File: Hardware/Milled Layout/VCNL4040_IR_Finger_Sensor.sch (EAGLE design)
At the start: 9 parts, among them U1 VCNL4040

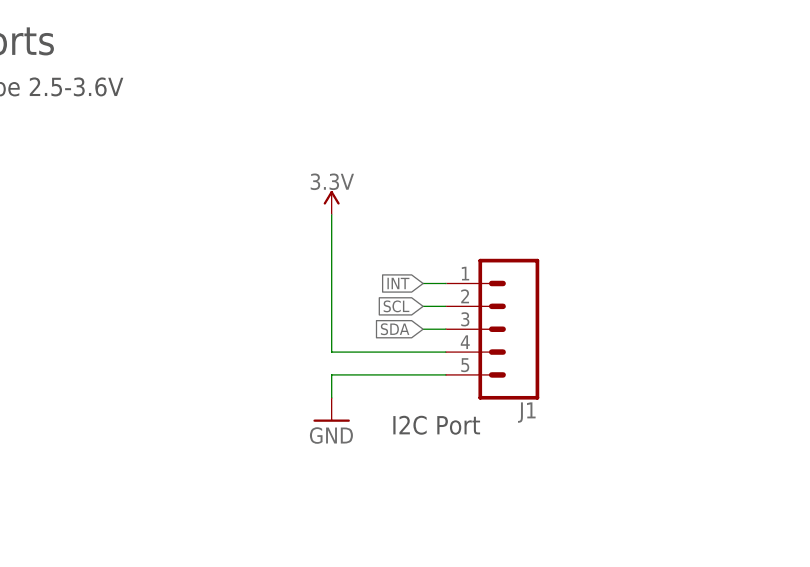
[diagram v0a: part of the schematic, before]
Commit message: Got rid of INT pin for Mill version
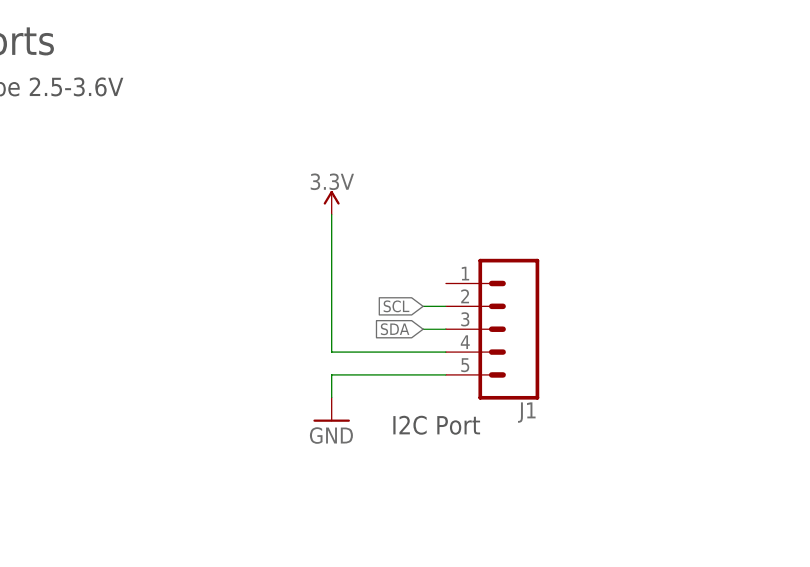
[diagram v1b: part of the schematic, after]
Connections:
- net INT: no longer J1.1
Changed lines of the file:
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@@
 <junction x="139.7" y="106.68"/>
-</segment>
-<segment>
-<wire x1="68.58" y1="33.02" x2="66.04" y2="33.02" width="0.1524" layer="91"/>
-<label x="66.04" y="33.02" size="1.27" layer="95" rot="R180" xref="yes"/>
-<pinref part="J1" gate="G$1" pin="1"/>
 </segment>
 </net>

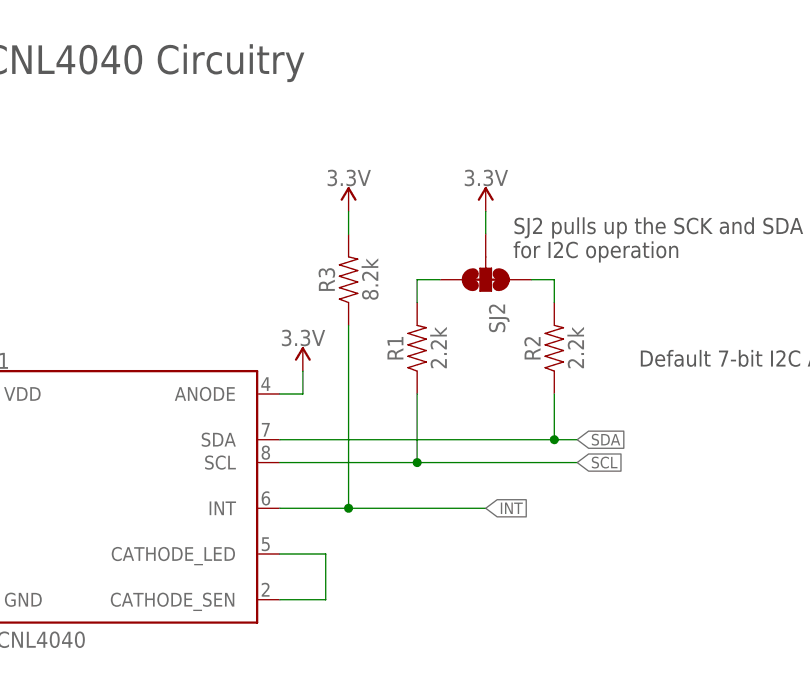
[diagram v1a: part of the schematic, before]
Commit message: New proto layout with no vias
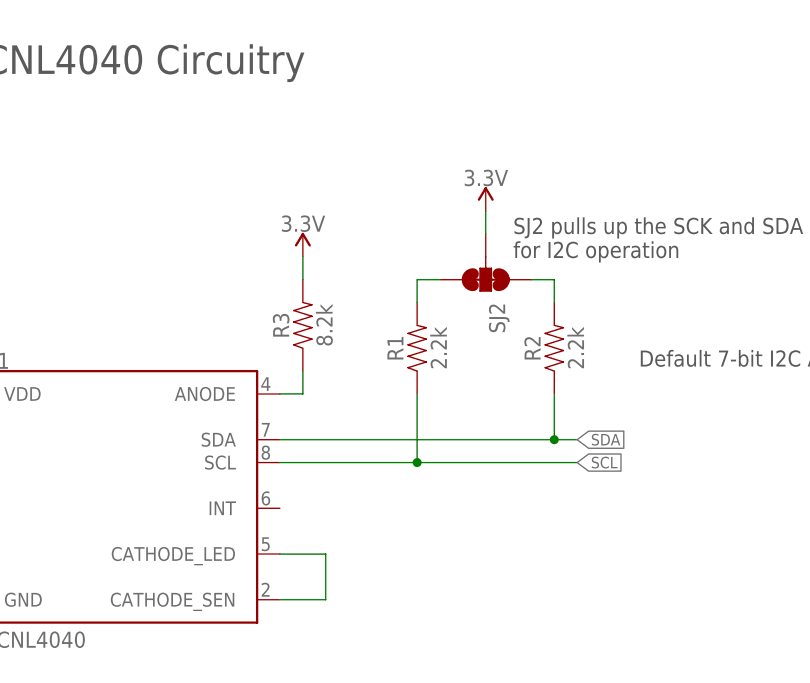
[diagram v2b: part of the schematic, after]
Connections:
- removed net INT: R3.1, U1.INT
- new net N$2: R3.1, U1.ANODE
- net 3.3V: no longer U1.ANODE
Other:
- moved on the sheet: R3
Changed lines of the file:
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@@
 <?xml version="1.0" encoding="utf-8"?>
 <!DOCTYPE eagle SYSTEM "eagle.dtd">
-<eagle version="7.6.0">
+<eagle version="7.7.0">
 <drawing>
 <settings>
@@
 <part name="J1" library="SparkFun-Connectors" deviceset="CONN_05" device=""/>
 <part name="R3" library="SparkFun-Resistors" deviceset="8.2KOHM" device="-0603-1/10W-5%" value="8.2k"/>
-<part name="SUPPLY4" library="SparkFun-PowerSymbols" deviceset="3.3V" device=""/>
 </parts>
 <sheets>
@@
 <instance part="SJ2" gate="G$1" x="154.94" y="132.08" rot="R270"/>
 <instance part="SUPPLY8" gate="G$1" x="55.88" y="40.64"/>
-<instance part="SUPPLY11" gate="G$1" x="134.62" y="121.92"/>
+<instance part="SUPPLY11" gate="G$1" x="134.62" y="134.62"/>
 <instance part="SUPPLY12" gate="G$1" x="154.94" y="139.7"/>
 <instance part="SUPPLY1" gate="G$1" x="93.98" y="121.92"/>
@@
 <instance part="U1" gate="G$1" x="114.3" y="109.22"/>
 <instance part="J1" gate="G$1" x="76.2" y="27.94" rot="R180"/>
-<instance part="R3" gate="G$1" x="139.7" y="132.08" rot="R90"/>
-<instance part="SUPPLY4" gate="G$1" x="139.7" y="139.7"/>
+<instance part="R3" gate="G$1" x="134.62" y="127" rot="R90"/>
 </instances>
 <busses>
@@
 </segment>
 </net>
-<net name="INT" class="0">
-<segment>
-<wire x1="132.08" y1="106.68" x2="139.7" y2="106.68" width="0.1524" layer="91"/>
-<label x="154.94" y="106.68" size="1.27" layer="95" xref="yes"/>
-<pinref part="U1" gate="G$1" pin="INT"/>
-<pinref part="R3" gate="G$1" pin="1"/>
-<wire x1="139.7" y1="106.68" x2="154.94" y2="106.68" width="0.1524" layer="91"/>
-<wire x1="139.7" y1="127" x2="139.7" y2="106.68" width="0.1524" layer="91"/>
-<junction x="139.7" y="106.68"/>
-</segment>
-</net>
 <net name="3.3V" class="0">
 <segment>
@@
 </segment>
 <segment>
+<pinref part="R3" gate="G$1" pin="2"/>
 <pinref part="SUPPLY11" gate="G$1" pin="3.3V"/>
-<pinref part="U1" gate="G$1" pin="ANODE"/>
-<wire x1="134.62" y1="121.92" x2="134.62" y2="119.38" width="0.1524" layer="91"/>
-<wire x1="134.62" y1="119.38" x2="132.08" y2="119.38" width="0.1524" layer="91"/>
-</segment>
-<segment>
-<pinref part="R3" gate="G$1" pin="2"/>
-<pinref part="SUPPLY4" gate="G$1" pin="3.3V"/>
-<wire x1="139.7" y1="137.16" x2="139.7" y2="139.7" width="0.1524" layer="91"/>
+<wire x1="134.62" y1="134.62" x2="134.62" y2="132.08" width="0.1524" layer="91"/>
 </segment>
 </net>
@@
 </segment>
 </net>
+<net name="N$2" class="0">
+<segment>
+<pinref part="U1" gate="G$1" pin="ANODE"/>
+<wire x1="134.62" y1="119.38" x2="132.08" y2="119.38" width="0.1524" layer="91"/>
+<pinref part="R3" gate="G$1" pin="1"/>
+<wire x1="134.62" y1="121.92" x2="134.62" y2="119.38" width="0.1524" layer="91"/>
+</segment>
+</net>

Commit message: Adding examples. Testing JST on milled layout.
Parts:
- removed R3: 8.2k, SparkFun-Resistors:8.2KOHM-0603-1/10W-5%
- removed SJ2: (no value), TestAperatures:JUMPER-PAD-3-NC_BY_TRACE
- added U$1, U$2: STAND-OFF, SparkX:STAND-OFF
- J1: device SparkFun-Connectors:CONN_05 -> SparkFun-Connectors:CONN_04SMD2
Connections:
- removed net N$2: R3.1, U1.ANODE
- removed net N$4: R2.2, SJ2.1
- removed net N$5: R1.2, SJ2.3
- net 3.3V: now also J1.2, R1.2, R2.2, U1.ANODE; no longer J1.4, R3.2, SJ2.2
- net GND: now also J1.1; no longer J1.5
- net SCL: now also J1.4; no longer J1.2
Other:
- note removed: "SJ2 pulls up the SCK and SDA lines for I2C operation"
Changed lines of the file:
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@@
 <part name="GND4" library="SparkFun" deviceset="GND" device=""/>
 <part name="C4" library="SparkFun-Capacitors" deviceset="0.1UF" device="-0603-25V-(+80/-20%)" value="0.1uF"/>
-<part name="SJ2" library="TestAperatures" deviceset="JUMPER-PAD-3-NC_BY_TRACE" device=""/>
 <part name="SUPPLY8" library="SparkFun-PowerSymbols" deviceset="3.3V" device=""/>
 <part name="SUPPLY11" library="SparkFun-PowerSymbols" deviceset="3.3V" device=""/>
@@
 <part name="GND8" library="SparkFun-PowerSymbols" deviceset="GND" device=""/>
 <part name="U1" library="SparkX" deviceset="VCNL4040" device=""/>
-<part name="J1" library="SparkFun-Connectors" deviceset="CONN_05" device=""/>
-<part name="R3" library="SparkFun-Resistors" deviceset="8.2KOHM" device="-0603-1/10W-5%" value="8.2k"/>
+<part name="U$1" library="SparkX" deviceset="STAND-OFF" device=""/>
+<part name="U$2" library="SparkX" deviceset="STAND-OFF" device=""/>
+<part name="J1" library="SparkFun-Connectors" deviceset="CONN_04" device="SMD2"/>
+<part name="SUPPLY4" library="SparkFun-PowerSymbols" deviceset="3.3V" device=""/>
 </parts>
 <sheets>
@@
 <text x="170.688" y="11.176" size="2.54" layer="94">Joel Bartlett</text>
 <text x="5.08" y="177.8" size="3.81" layer="97">VCNL4040 IR Finger Sensor Breakout</text>
-<text x="157.988" y="138.938" size="1.778" layer="97" align="top-left">SJ2 pulls up the SCK and SDA lines
-for I2C operation</text>
 <wire x1="0" y1="66.04" x2="147.32" y2="66.04" width="0.1524" layer="97" style="longdash"/>
 <wire x1="147.32" y1="66.04" x2="147.32" y2="35.56" width="0.1524" layer="97" style="longdash"/>
@@
 <instance part="GND4" gate="1" x="55.88" y="17.78"/>
 <instance part="C4" gate="G$1" x="73.66" y="106.68"/>
-<instance part="SJ2" gate="G$1" x="154.94" y="132.08" rot="R270"/>
 <instance part="SUPPLY8" gate="G$1" x="55.88" y="40.64"/>
-<instance part="SUPPLY11" gate="G$1" x="134.62" y="134.62"/>
-<instance part="SUPPLY12" gate="G$1" x="154.94" y="139.7"/>
+<instance part="SUPPLY11" gate="G$1" x="134.62" y="121.92"/>
+<instance part="SUPPLY12" gate="G$1" x="162.56" y="132.08"/>
 <instance part="SUPPLY1" gate="G$1" x="93.98" y="121.92"/>
 <instance part="SUPPLY2" gate="G$1" x="83.82" y="114.3"/>
@@
 <instance part="GND8" gate="1" x="83.82" y="99.06"/>
 <instance part="U1" gate="G$1" x="114.3" y="109.22"/>
-<instance part="J1" gate="G$1" x="76.2" y="27.94" rot="R180"/>
-<instance part="R3" gate="G$1" x="134.62" y="127" rot="R90"/>
+<instance part="U$1" gate="G$1" x="246.38" y="20.32"/>
+<instance part="U$2" gate="G$1" x="243.84" y="20.32"/>
+<instance part="J1" gate="G$1" x="73.66" y="25.4" rot="MR0"/>
+<instance part="SUPPLY4" gate="G$1" x="147.32" y="132.08"/>
 </instances>
 <busses>
@@
 <pinref part="GND4" gate="1" pin="GND"/>
 <wire x1="55.88" y1="20.32" x2="55.88" y2="22.86" width="0.1524" layer="91"/>
-<pinref part="J1" gate="G$1" pin="5"/>
+<pinref part="J1" gate="G$1" pin="1"/>
 </segment>
 </net>
@@
 <wire x1="68.58" y1="30.48" x2="66.04" y2="30.48" width="0.1524" layer="91"/>
 <label x="66.04" y="30.48" size="1.27" layer="95" rot="MR0" xref="yes"/>
-<pinref part="J1" gate="G$1" pin="2"/>
+<pinref part="J1" gate="G$1" pin="4"/>
 </segment>
 <segment>
@@
 </segment>
 </net>
-<net name="N$4" class="0">
-<segment>
-<pinref part="SJ2" gate="G$1" pin="1"/>
-<pinref part="R2" gate="G$1" pin="2"/>
-<wire x1="160.02" y1="132.08" x2="162.56" y2="132.08" width="0.1524" layer="91"/>
-<wire x1="162.56" y1="132.08" x2="162.56" y2="129.54" width="0.1524" layer="91"/>
-</segment>
-</net>
-<net name="N$5" class="0">
-<segment>
-<pinref part="SJ2" gate="G$1" pin="3"/>
-<pinref part="R1" gate="G$1" pin="2"/>
-<wire x1="149.86" y1="132.08" x2="147.32" y2="132.08" width="0.1524" layer="91"/>
-<wire x1="147.32" y1="132.08" x2="147.32" y2="129.54" width="0.1524" layer="91"/>
-</segment>
-</net>
 <net name="3.3V" class="0">
 <segment>
@@
 <wire x1="55.88" y1="40.64" x2="55.88" y2="25.4" width="0.1524" layer="91"/>
 <pinref part="SUPPLY8" gate="G$1" pin="3.3V"/>
-<pinref part="J1" gate="G$1" pin="4"/>
-</segment>
-<segment>
-<pinref part="SJ2" gate="G$1" pin="2"/>
-<wire x1="154.94" y1="139.7" x2="154.94" y2="137.16" width="0.1524" layer="91"/>
-<pinref part="SUPPLY12" gate="G$1" pin="3.3V"/>
+<pinref part="J1" gate="G$1" pin="2"/>
 </segment>
 <segment>
@@
 </segment>
 <segment>
-<pinref part="R3" gate="G$1" pin="2"/>
 <pinref part="SUPPLY11" gate="G$1" pin="3.3V"/>
-<wire x1="134.62" y1="134.62" x2="134.62" y2="132.08" width="0.1524" layer="91"/>
+<pinref part="U1" gate="G$1" pin="ANODE"/>
+<wire x1="134.62" y1="119.38" x2="132.08" y2="119.38" width="0.1524" layer="91"/>
+<wire x1="134.62" y1="121.92" x2="134.62" y2="119.38" width="0.1524" layer="91"/>
+</segment>
+<segment>
+<pinref part="R1" gate="G$1" pin="2"/>
+<wire x1="147.32" y1="132.08" x2="147.32" y2="129.54" width="0.1524" layer="91"/>
+<pinref part="SUPPLY4" gate="G$1" pin="3.3V"/>
+</segment>
+<segment>
+<pinref part="R2" gate="G$1" pin="2"/>
+<wire x1="162.56" y1="132.08" x2="162.56" y2="129.54" width="0.1524" layer="91"/>
+<pinref part="SUPPLY12" gate="G$1" pin="3.3V"/>
 </segment>
 </net>
@@
 </segment>
 </net>
-<net name="N$2" class="0">
-<segment>
-<pinref part="U1" gate="G$1" pin="ANODE"/>
-<wire x1="134.62" y1="119.38" x2="132.08" y2="119.38" width="0.1524" layer="91"/>
-<pinref part="R3" gate="G$1" pin="1"/>
-<wire x1="134.62" y1="121.92" x2="134.62" y2="119.38" width="0.1524" layer="91"/>
-</segment>
-</net>
